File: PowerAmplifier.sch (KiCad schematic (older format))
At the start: 41 parts, among them K1 РЭС60, P1 Filter disable, P2 INPUT, P3 POWER, P4 CLIP DETECTION, P5 OUT

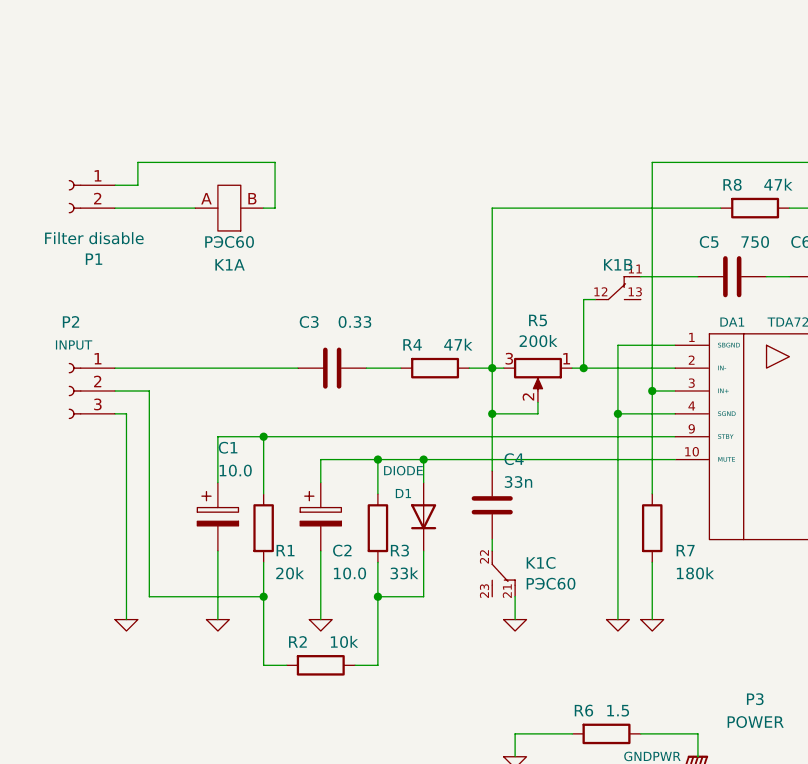
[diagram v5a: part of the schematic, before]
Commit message: Add footprints
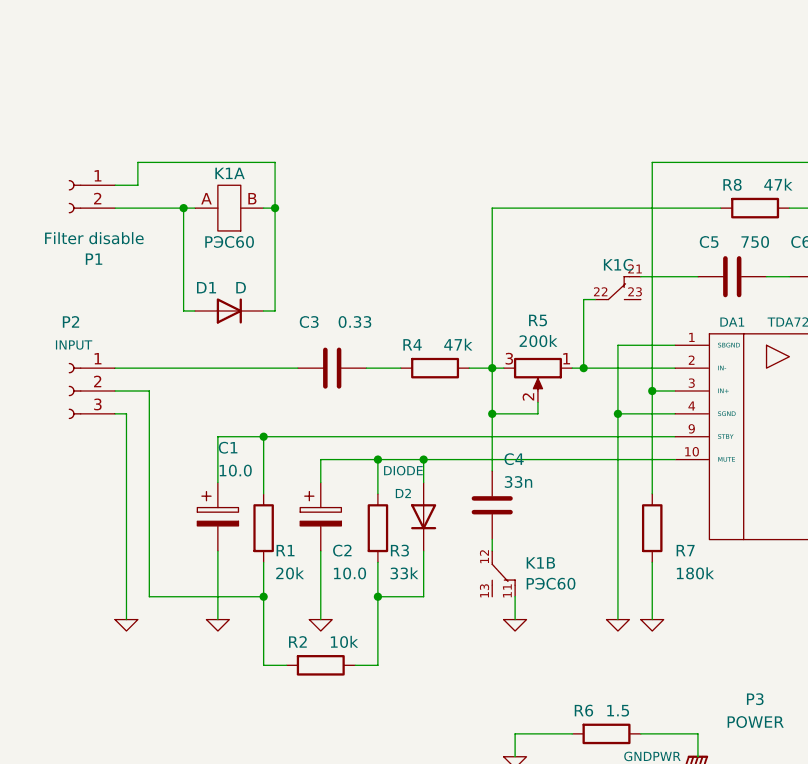
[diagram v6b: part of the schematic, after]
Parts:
- added D1: D, Diodes_ThroughHole:D_DO-15_P15.24mm_Horizontal, symbol Device:D
- C10: footprint Capacitors_ThroughHole:C_Rect_L31.5mm_W13.0mm_P27.50mm_MKS4 -> Capacitors_ThroughHole:CP_Axial_L29.0mm_D10.0mm_P35.00mm_Horizontal
- C11: footprint Capacitors_ThroughHole:C_Rect_L41.5mm_W15.0mm_P37.50mm_MKS4 -> Capacitors_ThroughHole:C_Rect_L24.0mm_W12.2mm_P22.50mm_MKT
- C12, C19: footprint Capacitors_ThroughHole:C_Rect_L13.5mm_W5.0mm_P10.00mm_FKS3_FKP3_MKS4 -> Capacitors_ThroughHole:C_Rect_L24.0mm_W12.2mm_P22.50mm_MKT
- C13, C16: footprint Capacitors_ThroughHole:CP_Radial_D10.0mm_P3.50mm -> Capacitors_ThroughHole:CP_Radial_D10.0mm_P2.50mm_P5.00mm
- C14: footprint Capacitors_ThroughHole:C_Rect_L41.5mm_W15.0mm_P37.50mm_MKS4 -> Capacitors_ThroughHole:C_Rect_L18.0mm_W8.0mm_P15.00mm_FKS3_FKP3
- C15: footprint Capacitors_ThroughHole:C_Rect_L13.0mm_W6.0mm_P10.00mm_FKS3_FKP3_MKS4 -> Capacitors_ThroughHole:C_Rect_L18.0mm_W8.0mm_P15.00mm_FKS3_FKP3
- C17: footprint Capacitors_ThroughHole:C_Rect_L16.5mm_W6.0mm_P15.00mm_MKT -> Capacitors_ThroughHole:C_Rect_L18.0mm_W8.0mm_P15.00mm_FKS3_FKP3
- C18, C8: footprint Capacitors_ThroughHole:CP_Radial_D13.0mm_P5.00mm -> Capacitors_ThroughHole:CP_Radial_D10.0mm_P5.00mm_P7.50mm
- C4: footprint Capacitors_ThroughHole:C_Rect_L13.5mm_W5.0mm_P10.00mm_FKS3_FKP3_MKS4 -> Capacitors_ThroughHole:C_Rect_L16.5mm_W9.0mm_P15.00mm_MKT
- C5: footprint Capacitors_ThroughHole:C_Rect_L10.0mm_W4.0mm_P7.50mm_MKS4 -> Capacitors_ThroughHole:C_Rect_L16.5mm_W7.3mm_P15.00mm_MKT
- C6: footprint (none) -> Capacitors_ThroughHole:C_Rect_L16.5mm_W7.3mm_P15.00mm_MKT
- C7: footprint Capacitors_ThroughHole:C_Rect_L33.0mm_W13.0mm_P27.50mm_MKS4 -> Capacitors_ThroughHole:CP_Axial_L29.0mm_D10.0mm_P35.00mm_Horizontal
- C9: footprint Capacitors_ThroughHole:CP_Radial_D8.0mm_P3.50mm -> Capacitors_ThroughHole:CP_Radial_D10.0mm_P2.50mm_P5.00mm
- D2: renamed from D1; footprint Diodes_ThroughHole:D_DO-41_SOD81_P10.16mm_Horizontal -> Diodes_ThroughHole:D_DO-15_P15.24mm_Horizontal
- P1: footprint (none) -> Pin_Headers:Pin_Header_Straight_1x02_Pitch2.54mm
- R5: footprint (none) -> Potentiometers:Potentiometer_Trimmer_Bourns_3296Y
- RV1: footprint Potentiometers:Potentiometer_Trimmer_Piher_PT-10v10_Horizontal_Px10.0mm_Py5.0mm -> Potentiometers:Potentiometer_Trimmer_Bourns_3296Y
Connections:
- net GND: now also K1.11; no longer K1.21
- net at DA1.2 (IN-), R5.1: now also K1.22; no longer K1.12
- net at C4.2: now also K1.12; no longer K1.22
- net at C5.2: now also K1.21; no longer K1.11
- net at K1.B, P1.1 (Pin_1): now also D1.1 (K)
- net at K1.A, P1.2 (Pin_2): now also D1.2 (A)
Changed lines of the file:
@@
 F 0 "RV1" H 7650 3500 50  0000 C CNN
 F 1 "200" H 7650 3400 50  0000 C CNN
-F 2 "Potentiometers:Potentiometer_Trimmer_Piher_PT-10v10_Horizontal_Px10.0mm_Py5.0mm" H 7550 3250 60  0001 C CNN
+F 2 "Potentiometers:Potentiometer_Trimmer_Bourns_3296Y" H 7550 3250 60  0001 C CNN
 F 3 "" H 7550 3250 60  0001 C CNN
 	1    7550 3250
@@
 F 0 "C9" H 6250 3400 50  0000 C CNN
 F 1 "100.0" H 6300 3300 50  0000 C CNN
-F 2 "Capacitors_ThroughHole:CP_Radial_D8.0mm_P3.50mm" H 6150 3200 60  0001 C CNN
+F 2 "Capacitors_ThroughHole:CP_Radial_D10.0mm_P2.50mm_P5.00mm" H 6150 3200 60  0001 C CNN
 F 3 "" H 6150 3200 60  0001 C CNN
 	1    6150 3200
@@
 P 4900 2450
 AR Path="/58343792" Ref="C5"  Part="1"
-AR Path="/5833169E/58343792" Ref="C96"  Part="1"
+AR Path="/5833169E/58343792" Ref="C?"  Part="1"
 F 0 "C5" V 4750 2350 50  0000 C CNN
 F 1 "750" V 4750 2550 50  0000 C CNN
-F 2 "Capacitors_ThroughHole:C_Rect_L10.0mm_W4.0mm_P7.50mm_MKS4" H 4900 2450 60  0001 C CNN
+F 2 "Capacitors_ThroughHole:C_Rect_L16.5mm_W7.3mm_P15.00mm_MKT" H 4900 2450 60  0001 C CNN
 F 3 "" H 4900 2450 60  0001 C CNN
 	1    4900 2450
@@
 P 6450 3200
 AR Path="/58345D7D" Ref="C11"  Part="1"
-AR Path="/5833169E/58345D7D" Ref="C99"  Part="1"
+AR Path="/5833169E/58345D7D" Ref="C?"  Part="1"
 F 0 "C11" H 6400 3000 50  0000 R CNN
 F 1 "1.0" H 6400 3100 50  0000 R CNN
-F 2 "Capacitors_ThroughHole:C_Rect_L41.5mm_W15.0mm_P37.50mm_MKS4" H 6450 3200 60  0001 C CNN
+F 2 "Capacitors_ThroughHole:C_Rect_L24.0mm_W12.2mm_P22.50mm_MKT" H 6450 3200 60  0001 C CNN
 F 3 "" H 6450 3200 60  0001 C CNN
 	1    6450 3200
@@
 P 6950 2350
 AR Path="/58341C01" Ref="C14"  Part="1"
-AR Path="/5833169E/58341C01" Ref="C102"  Part="1"
+AR Path="/5833169E/58341C01" Ref="C?"  Part="1"
 F 0 "C14" H 7000 2550 50  0000 L CNN
 F 1 "0.1" H 7000 2450 50  0000 L CNN
-F 2 "Capacitors_ThroughHole:C_Rect_L41.5mm_W15.0mm_P37.50mm_MKS4" H 6950 2350 60  0001 C CNN
+F 2 "Capacitors_ThroughHole:C_Rect_L18.0mm_W8.0mm_P15.00mm_FKS3_FKP3" H 6950 2350 60  0001 C CNN
 F 3 "" H 6950 2350 60  0001 C CNN
 	1    6950 2350
@@
 $EndComp
 $Comp
-L Device:D D1
+L Device:D D2
 U 1 1 58348115
 P 3550 3500
-F 0 "D1" V 3650 3550 40  0000 L CNN
+F 0 "D2" V 3650 3550 40  0000 L CNN
 F 1 "DIODE" V 3750 3500 40  0000 L CNN
-F 2 "Diodes_ThroughHole:D_DO-41_SOD81_P10.16mm_Horizontal" H 3550 3500 60  0001 C CNN
+F 2 "Diodes_ThroughHole:D_DO-15_P15.24mm_Horizontal" H 3550 3500 60  0001 C CNN
 F 3 "" H 3550 3500 60  0001 C CNN
 	1    3550 3500
@@
 F 0 "C8" H 5950 4100 50  0000 L CNN
 F 1 "1000.0" H 5800 4200 50  0000 L CNN
-F 2 "Capacitors_ThroughHole:CP_Radial_D13.0mm_P5.00mm" H 6100 4300 60  0001 C CNN
+F 2 "Capacitors_ThroughHole:CP_Radial_D10.0mm_P5.00mm_P7.50mm" H 6100 4300 60  0001 C CNN
 F 3 "" H 6100 4300 60  0001 C CNN
 	1    6100 4300
@@
 F 0 "C13" H 6650 4100 50  0000 L CNN
 F 1 "220.0" H 6550 4200 50  0000 L CNN
-F 2 "Capacitors_ThroughHole:CP_Radial_D10.0mm_P3.50mm" H 6800 4300 60  0001 C CNN
+F 2 "Capacitors_ThroughHole:CP_Radial_D10.0mm_P2.50mm_P5.00mm" H 6800 4300 60  0001 C CNN
 F 3 "" H 6800 4300 60  0001 C CNN
 	1    6800 4300
@@
 F 0 "C16" H 7550 4500 50  0000 L CNN
 F 1 "220.0" H 7550 4400 50  0000 L CNN
-F 2 "Capacitors_ThroughHole:CP_Radial_D10.0mm_P3.50mm" H 7500 4300 60  0001 C CNN
+F 2 "Capacitors_ThroughHole:CP_Radial_D10.0mm_P2.50mm_P5.00mm" H 7500 4300 60  0001 C CNN
 F 3 "" H 7500 4300 60  0001 C CNN
 	1    7500 4300
@@
 F 0 "C18" H 8250 4500 50  0000 L CNN
 F 1 "1000.0" H 8250 4400 50  0000 L CNN
-F 2 "Capacitors_ThroughHole:CP_Radial_D13.0mm_P5.00mm" H 8200 4300 60  0001 C CNN
+F 2 "Capacitors_ThroughHole:CP_Radial_D10.0mm_P5.00mm_P7.50mm" H 8200 4300 60  0001 C CNN
 F 3 "" H 8200 4300 60  0001 C CNN
 	1    8200 4300
@@
 P 6450 4300
 AR Path="/5834CA0A" Ref="C12"  Part="1"
-AR Path="/5833169E/5834CA0A" Ref="C100"  Part="1"
+AR Path="/5833169E/5834CA0A" Ref="C?"  Part="1"
 F 0 "C12" H 6500 4500 50  0000 L CNN
 F 1 "1.0" H 6500 4400 50  0000 L CNN
-F 2 "Capacitors_ThroughHole:C_Rect_L13.5mm_W5.0mm_P10.00mm_FKS3_FKP3_MKS4" H 6450 4300 60  0001 C CNN
+F 2 "Capacitors_ThroughHole:C_Rect_L24.0mm_W12.2mm_P22.50mm_MKT" H 6450 4300 60  0001 C CNN
 F 3 "" H 6450 4300 60  0001 C CNN
 	1    6450 4300
@@
 P 7150 4300
 AR Path="/5834CA70" Ref="C15"  Part="1"
-AR Path="/5833169E/5834CA70" Ref="C103"  Part="1"
+AR Path="/5833169E/5834CA70" Ref="C?"  Part="1"
 F 0 "C15" H 7200 4500 50  0000 L CNN
 F 1 "0.1" H 7200 4400 50  0000 L CNN
-F 2 "Capacitors_ThroughHole:C_Rect_L13.0mm_W6.0mm_P10.00mm_FKS3_FKP3_MKS4" H 7150 4300 60  0001 C CNN
+F 2 "Capacitors_ThroughHole:C_Rect_L18.0mm_W8.0mm_P15.00mm_FKS3_FKP3" H 7150 4300 60  0001 C CNN
 F 3 "" H 7150 4300 60  0001 C CNN
 	1    7150 4300
@@
 P 7850 4300
 AR Path="/5834CAC8" Ref="C17"  Part="1"
-AR Path="/5833169E/5834CAC8" Ref="C106"  Part="1"
+AR Path="/5833169E/5834CAC8" Ref="C?"  Part="1"
 F 0 "C17" H 7900 4500 50  0000 L CNN
 F 1 "0.1" H 7900 4400 50  0000 L CNN
-F 2 "Capacitors_ThroughHole:C_Rect_L16.5mm_W6.0mm_P15.00mm_MKT" H 7850 4300 60  0001 C CNN
+F 2 "Capacitors_ThroughHole:C_Rect_L18.0mm_W8.0mm_P15.00mm_FKS3_FKP3" H 7850 4300 60  0001 C CNN
 F 3 "" H 7850 4300 60  0001 C CNN
 	1    7850 4300
@@
 P 8550 4300
 AR Path="/5834CB82" Ref="C19"  Part="1"
-AR Path="/5833169E/5834CB82" Ref="C108"  Part="1"
+AR Path="/5833169E/5834CB82" Ref="C?"  Part="1"
 F 0 "C19" H 8600 4500 50  0000 L CNN
 F 1 "1.0" H 8600 4400 50  0000 L CNN
-F 2 "Capacitors_ThroughHole:C_Rect_L13.5mm_W5.0mm_P10.00mm_FKS3_FKP3_MKS4" H 8550 4300 60  0001 C CNN
+F 2 "Capacitors_ThroughHole:C_Rect_L24.0mm_W12.2mm_P22.50mm_MKT" H 8550 4300 60  0001 C CNN
 F 3 "" H 8550 4300 60  0001 C CNN
 	1    8550 4300
@@
 P 3150 2850
 AR Path="/58342B6B" Ref="C3"  Part="1"
-AR Path="/5833169E/58342B6B" Ref="C94"  Part="1"
+AR Path="/5833169E/58342B6B" Ref="C?"  Part="1"
 F 0 "C3" V 2950 2750 50  0000 C CNN
 F 1 "0.33" V 2950 2950 50  0000 C CNN
@@
 P 5600 1950
 AR Path="/5D76D768" Ref="C7"  Part="1"
-AR Path="/5833169E/5D76D768" Ref="C104"  Part="1"
+AR Path="/5833169E/5D76D768" Ref="C?"  Part="1"
 F 0 "C7" V 5450 1850 50  0000 C CNN
 F 1 "0.15" V 5450 2050 50  0000 C CNN
-F 2 "Capacitors_ThroughHole:C_Rect_L33.0mm_W13.0mm_P27.50mm_MKS4" H 5600 1950 60  0001 C CNN
+F 2 "Capacitors_ThroughHole:CP_Axial_L29.0mm_D10.0mm_P35.00mm_Horizontal" H 5600 1950 60  0001 C CNN
 F 3 "" H 5600 1950 60  0001 C CNN
 	1    5600 1950
@@
 P 6250 2400
 AR Path="/5D77D443" Ref="C10"  Part="1"
-AR Path="/5833169E/5D77D443" Ref="C109"  Part="1"
+AR Path="/5833169E/5D77D443" Ref="C?"  Part="1"
 F 0 "C10" H 6500 2350 50  0000 C CNN
 F 1 "0.15" H 6500 2450 50  0000 C CNN
-F 2 "Capacitors_ThroughHole:C_Rect_L31.5mm_W13.0mm_P27.50mm_MKS4" H 6250 2400 60  0001 C CNN
+F 2 "Capacitors_ThroughHole:CP_Axial_L29.0mm_D10.0mm_P35.00mm_Horizontal" H 6250 2400 60  0001 C CNN
 F 3 "" H 6250 2400 60  0001 C CNN
 	1    6250 2400
@@
 P 3850 3450
 AR Path="/58342AF7" Ref="C4"  Part="1"
-AR Path="/5833169E/58342AF7" Ref="C92"  Part="1"
+AR Path="/5833169E/58342AF7" Ref="C?"  Part="1"
 F 0 "C4" H 3900 3650 50  0000 L CNN
 F 1 "33n" H 3900 3550 50  0000 L CNN
-F 2 "Capacitors_ThroughHole:C_Rect_L13.5mm_W5.0mm_P10.00mm_FKS3_FKP3_MKS4" H 3850 3450 60  0001 C CNN
+F 2 "Capacitors_ThroughHole:C_Rect_L16.5mm_W9.0mm_P15.00mm_MKT" H 3850 3450 60  0001 C CNN
 F 3 "" H 3850 3450 60  0001 C CNN
 	1    3850 3450
@@
 F 0 "R5" V 3843 2850 50  0000 C CNN
 F 1 "200k" V 3934 2850 50  0000 C CNN
-F 2 "" H 4050 2850 50  0001 C CNN
+F 2 "Potentiometers:Potentiometer_Trimmer_Bourns_3296Y" H 4050 2850 50  0001 C CNN
 F 3 "~" H 4050 2850 50  0001 C CNN
 	1    4050 2850
@@
 F 0 "C6" V 5150 2350 50  0000 C CNN
 F 1 "750" V 5150 2550 50  0000 C CNN
-F 2 "" H 5338 2300 50  0001 C CNN
+F 2 "Capacitors_ThroughHole:C_Rect_L16.5mm_W7.3mm_P15.00mm_MKT" H 5338 2300 50  0001 C CNN
 F 3 "~" H 5300 2450 50  0001 C CNN
 	1    5300 2450
@@
 U 1 1 6029EEBB
 P 2700 2150
-F 0 "K1" H 2700 2400 50  0000 C CNN
+F 0 "K1" H 2700 2000 50  0000 C CNN
 F 1 "РЭС60" H 2700 2300 50  0000 C CNN
 F 2 "РЭС60:РЭС60" H 2698 2150 50  0001 C CNN
@@
 $Comp
 L рэс60:РЭС60 K1
-U 2 1 602A1FB7
+U 3 1 602A1FB7
 P 4400 2550
 F 0 "K1" H 4400 2700 50  0000 C CNN
@@
 F 2 "РЭС60:РЭС60" H 4398 2550 50  0001 C CNN
 F 3 "" H 4398 2550 50  0001 C CNN
-	2    4400 2550
+	3    4400 2550
 	1    0    0    -1
 $EndComp
@@
 F 0 "P1" H 1892 1725 50  0000 C CNN
 F 1 "Filter disable" H 1892 1816 50  0000 C CNN
-F 2 "" H 2000 2050 50  0001 C CNN
+F 2 "Pin_Headers:Pin_Header_Straight_1x02_Pitch2.54mm" H 2000 2050 50  0001 C CNN
 F 3 "~" H 2000 2050 50  0001 C CNN
 	1    2000 2050
@@
 $EndComp
 Wire Wire Line
-	2550 2150 2200 2150
+	2550 2150 2500 2150
 Wire Wire Line
 	2850 2150 2900 2150
@@
 $Comp
 L рэс60:РЭС60 K1
-U 3 1 6013B7F1
+U 2 1 6013B7F1
 P 3850 3750
 F 0 "K1" V 3804 3894 50  0000 L CNN
@@
 F 2 "РЭС60:РЭС60" H 3848 3750 50  0001 C CNN
 F 3 "" H 3848 3750 50  0001 C CNN
-	3    3850 3750
+	2    3850 3750
 	0    1    1    0
 $EndComp
+$Comp
+L Device:D D1
+U 1 1 6019B9E4
+P 2700 2600
+F 0 "D1" H 2800 2500 50  0000 C CNN
+F 1 "D" H 2650 2500 50  0000 C CNN
+F 2 "Diodes_ThroughHole:D_DO-15_P15.24mm_Horizontal" H 2700 2600 50  0001 C CNN
+F 3 "~" H 2700 2600 50  0001 C CNN
+	1    2700 2600
+	-1   0    0    1
+$EndComp
+Wire Wire Line
+	2850 2600 2900 2600
+Wire Wire Line
+	2900 2600 2900 2150
+Connection ~ 2900 2150
+Wire Wire Line
+	2550 2600 2500 2600
+Wire Wire Line
+	2500 2600 2500 2150
+Connection ~ 2500 2150
+Wire Wire Line
+	2500 2150 2200 2150
 $EndSCHEMATC
